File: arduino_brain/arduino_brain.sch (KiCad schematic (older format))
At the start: 42 parts, among them U1 R-78B5.0-1.5

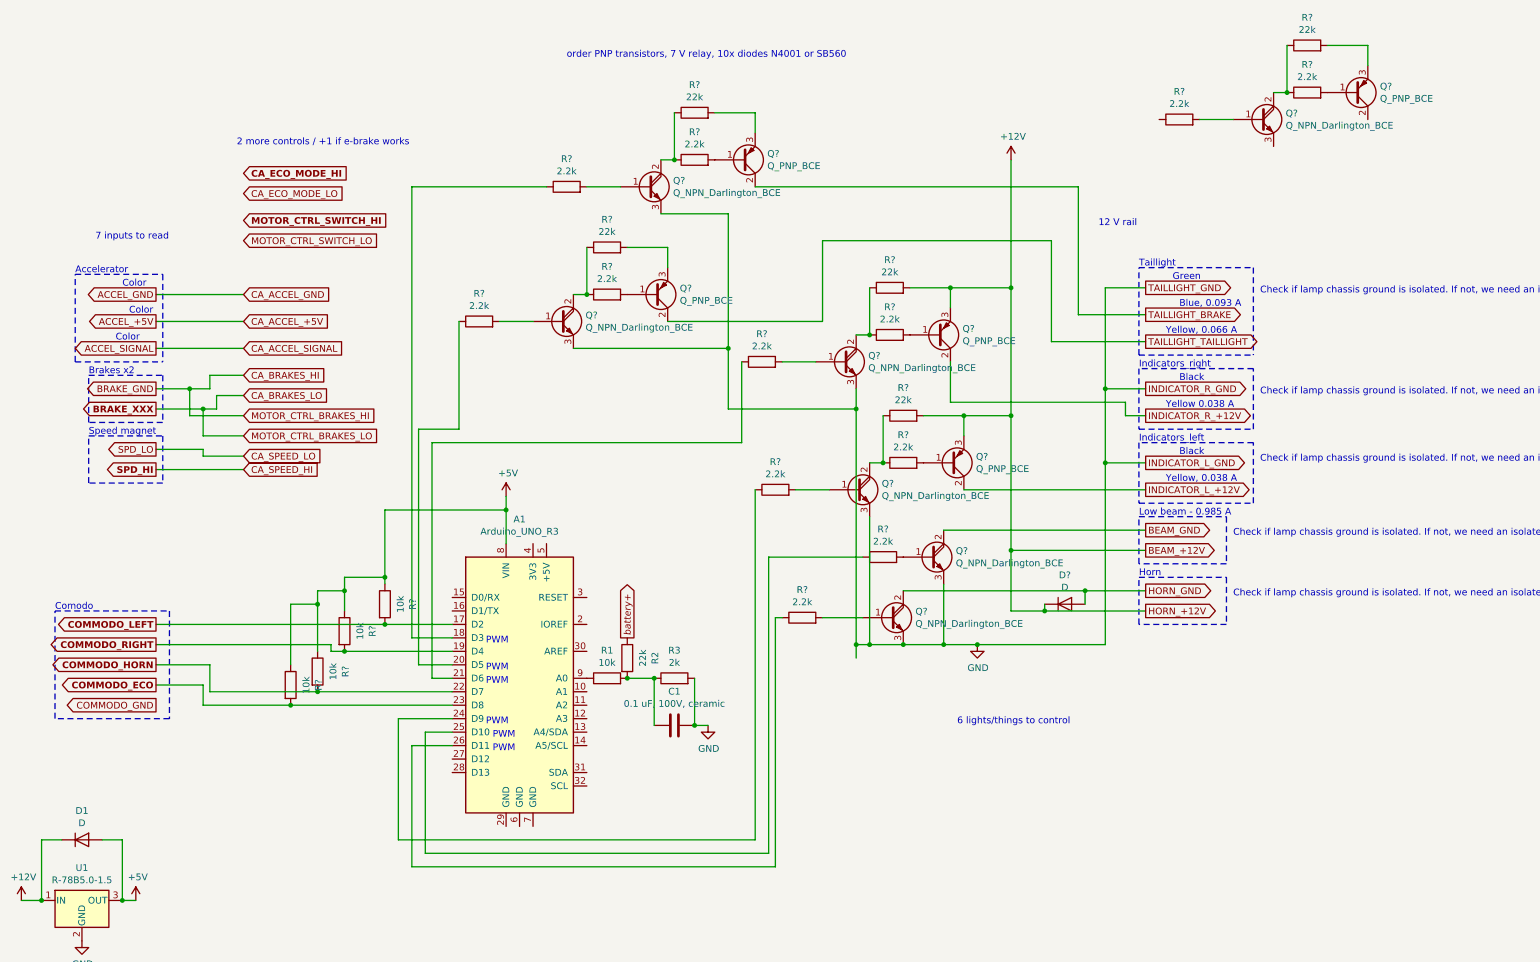
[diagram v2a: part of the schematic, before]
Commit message: Added 12V switching regulator, eco mode control and cleaned schematic
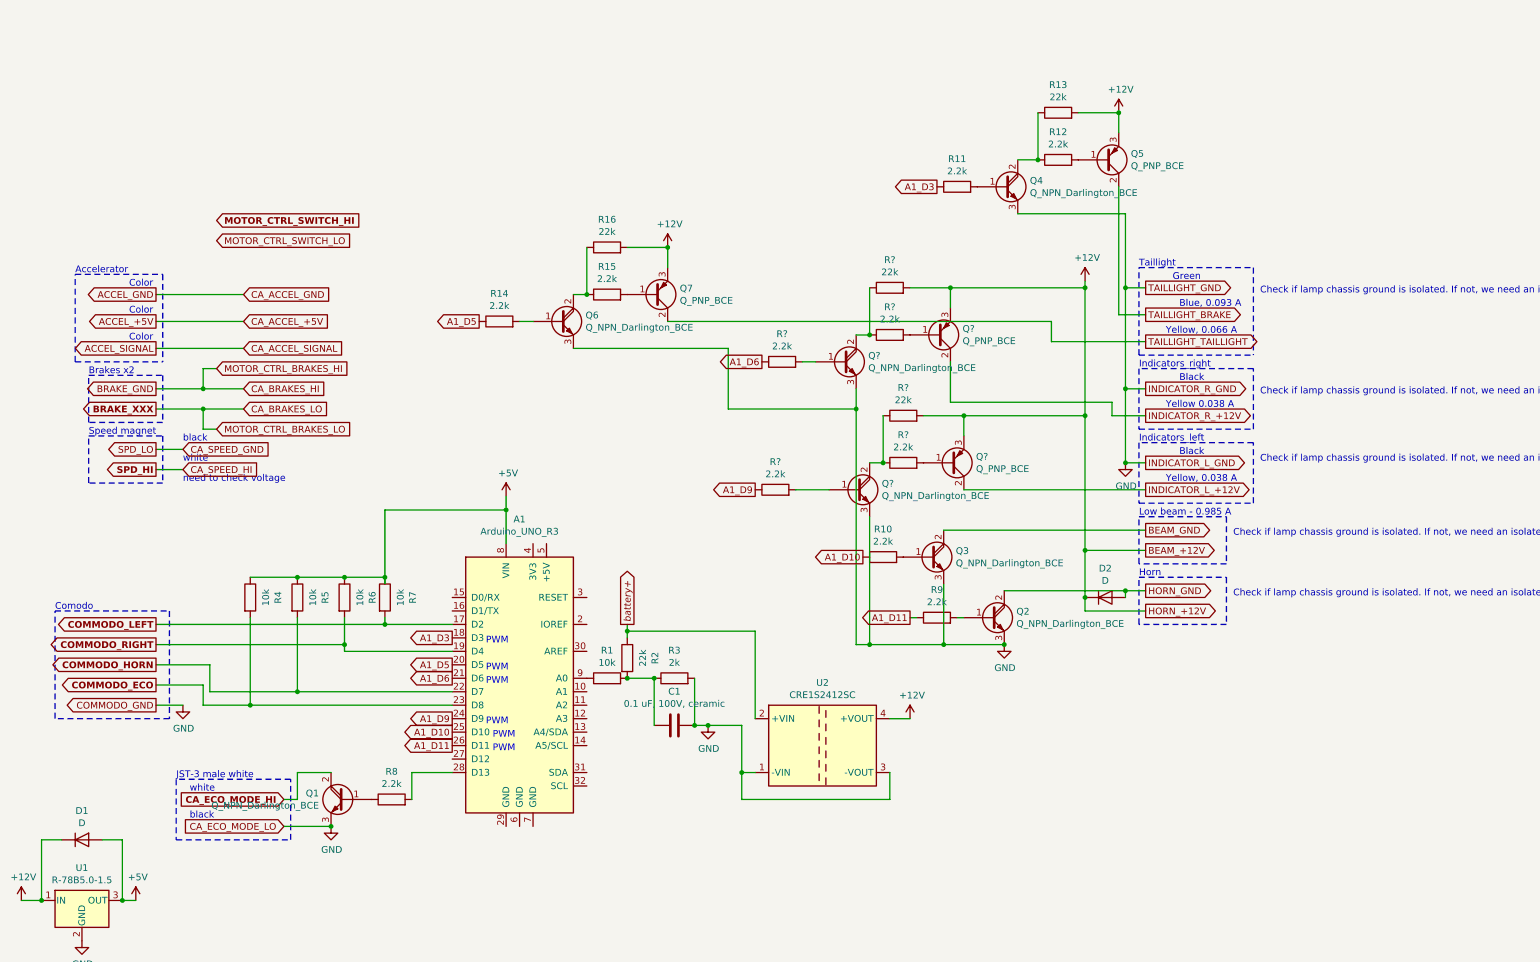
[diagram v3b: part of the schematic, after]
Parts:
- removed Q?: Q_NPN_Darlington_BCE, symbol Device:Q_NPN_Darlington_BCE
- removed Q?: Q_PNP_BCE, symbol Device:Q_PNP_BCE
- removed R? (x2): 2.2k, symbol Device:R
- removed R?: 22k, symbol Device:R
- added Q1: Q_NPN_Darlington_BCE, symbol Device:Q_NPN_Darlington_BCE
- added R8: 2.2k, symbol Device:R
- added U2: CRE1S2412SC, Converter_DCDC:Converter_DCDC_muRata_CRE1xxxxxxSC_THT, symbol Regulator_Switching:CRE1S2412SC
- gave numbers to parts that had none: 19
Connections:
- net +12V: now also Q5.3 (E), Q7.3 (E), R13.2, R16.2, U2.4 (+VOUT)
- net CA_ECO_MODE_HI: now also Q1.2 (C)
- net GND: now also Q1.3 (E), U2.1 (-VIN), U2.3 (-VOUT)
- net battery+: now also U2.2 (+VIN)
- net A1_D9: now reaches A1.24 (D9), R?.1
- net A1_D11: now reaches A1.26 (D11), R9.1
- net A1_D10: now reaches A1.25 (D10), R10.1
- net A1_D6: now reaches A1.21 (D6), R?.1
- net A1_D3: now reaches A1.18 (D3), R11.1
- net A1_D5: now reaches A1.20 (D5), R14.1
- net at A1.28 (D13): now also R8.2
- new net: Q1.1 (B), R8.1
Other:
- note added: "JST-3 male white"
- note added: "black"
- note added: "need to check voltage"
- note added: "white"
- note removed: "12 V rail"
- note removed: "2 more controls / +1 if e-brake works"
- note removed: "6 lights/things to control"
- note removed: "7 inputs to read"
- note removed: "order PNP transistors, 7 V relay, 10x diodes N4001 or SB560"
- moved on the sheet: D2, Q2, Q4, Q5, R11, R12, R13, R14, R4, R5, R6, R7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

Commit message: Cleaned up the notations
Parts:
- gave numbers to parts that had none: 11
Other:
- note added: "Black (2)"
- note added: "Green (3)"
- note added: "JST-3-F black"
- note added: "JST-3-F white"
- note added: "Red (1)"
- note added: "TODO: \n- wire the speed sensor\n- wire the start/stop"
- note added: "black (2)"
- note added: "white (3)"
- note removed: "9 free I/O\n15 I/O to have"
- note removed: "JST-3 male white"
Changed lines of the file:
@@
 $EndDescr
 $Comp
-L MCU_Module:Arduino_UNO_R3 A?
+L MCU_Module:Arduino_UNO_R3 A2
 U 1 1 5DFDE4CB
 P -1750 6050
-F 0 "A?" H -1750 7231 50  0000 C CNN
+F 0 "A2" H -1750 7231 50  0000 C CNN
 F 1 "Arduino_UNO_R3" H -1750 7140 50  0000 C CNN
 F 2 "Module:Arduino_UNO_R3" H -1600 5000 50  0001 L CNN
@@
 Text GLabel 1650 5700 0    50   Output ~ 0
 COMMODO_GND
-Text Notes -1100 5050 0    50   ~ 0
-9 free I/O\n15 I/O to have
 Text GLabel -2150 8050 2    50   Input ~ 0
 BLUEFRUIT_MOSI
@@
 	9000 5000 8550 5000
 $Comp
-L Device:Q_NPN_Darlington_BCE Q?
+L Device:Q_NPN_Darlington_BCE Q10
 U 1 1 5E0ABF98
 P 6850 4100
-F 0 "Q?" H 7040 4146 50  0000 L CNN
+F 0 "Q10" H 7040 4146 50  0000 L CNN
 F 1 "Q_NPN_Darlington_BCE" H 7040 4055 50  0000 L CNN
 F 2 "" H 7050 4200 50  0001 C CNN
@@
 $EndComp
 $Comp
-L Device:R R?
+L Device:R R20
 U 1 1 5E0AE97B
 P 6250 4100
-F 0 "R?" V 6457 4100 50  0000 C CNN
+F 0 "R20" V 6457 4100 50  0000 C CNN
 F 1 "2.2k" V 6366 4100 50  0000 C CNN
 F 2 "" V 6180 4100 50  0001 C CNN
@@
 Check if lamp chassis ground is isolated. If not, we need an isolated ground (not connecting battery ground with chassis ground!!!)
 $Comp
-L Device:Q_PNP_BCE Q?
+L Device:Q_PNP_BCE Q11
 U 1 1 5E0EA248
 P 7550 3900
-F 0 "Q?" H 7740 3854 50  0000 L CNN
+F 0 "Q11" H 7740 3854 50  0000 L CNN
 F 1 "Q_PNP_BCE" H 7740 3945 50  0000 L CNN
 F 2 "" H 7750 4000 50  0001 C CNN
@@
 $EndComp
 $Comp
-L Device:R R?
+L Device:R R21
 U 1 1 5E0EAF2D
 P 7200 3900
-F 0 "R?" V 7407 3900 50  0000 C CNN
+F 0 "R21" V 7407 3900 50  0000 C CNN
 F 1 "2.2k" V 7316 3900 50  0000 C CNN
 F 2 "" V 7130 3900 50  0001 C CNN
@@
 	7050 3900 6950 3900
 $Comp
-L Device:R R?
+L Device:R R22
 U 1 1 5E0FEFBE
 P 7200 3550
-F 0 "R?" V 7407 3550 50  0000 C CNN
+F 0 "R22" V 7407 3550 50  0000 C CNN
 F 1 "22k" V 7316 3550 50  0000 C CNN
 F 2 "" V 7130 3550 50  0001 C CNN
@@
 	7650 4100 9000 4100
 $Comp
-L Device:Q_NPN_Darlington_BCE Q?
+L Device:Q_NPN_Darlington_BCE Q8
 U 1 1 5E10C4F3
 P 6750 3150
-F 0 "Q?" H 6940 3196 50  0000 L CNN
+F 0 "Q8" H 6940 3196 50  0000 L CNN
 F 1 "Q_NPN_Darlington_BCE" H 6940 3105 50  0000 L CNN
 F 2 "" H 6950 3250 50  0001 C CNN
@@
 $EndComp
 $Comp
-L Device:R R?
+L Device:R R17
 U 1 1 5E10C4FD
 P 6300 3150
-F 0 "R?" V 6507 3150 50  0000 C CNN
+F 0 "R17" V 6507 3150 50  0000 C CNN
 F 1 "2.2k" V 6416 3150 50  0000 C CNN
 F 2 "" V 6230 3150 50  0001 C CNN
@@
 	6450 3150 6550 3150
 $Comp
-L Device:Q_PNP_BCE Q?
+L Device:Q_PNP_BCE Q9
 U 1 1 5E10C508
 P 7450 2950
-F 0 "Q?" H 7640 2904 50  0000 L CNN
+F 0 "Q9" H 7640 2904 50  0000 L CNN
 F 1 "Q_PNP_BCE" H 7640 2995 50  0000 L CNN
 F 2 "" H 7650 3050 50  0001 C CNN
@@
 $EndComp
 $Comp
-L Device:R R?
+L Device:R R18
 U 1 1 5E10C512
 P 7100 2950
-F 0 "R?" V 7307 2950 50  0000 C CNN
+F 0 "R18" V 7307 2950 50  0000 C CNN
 F 1 "2.2k" V 7216 2950 50  0000 C CNN
 F 2 "" V 7030 2950 50  0001 C CNN
@@
 	6950 2950 6850 2950
 $Comp
-L Device:R R?
+L Device:R R19
 U 1 1 5E10C51D
 P 7100 2600
-F 0 "R?" V 7307 2600 50  0000 C CNN
+F 0 "R19" V 7307 2600 50  0000 C CNN
 F 1 "22k" V 7216 2600 50  0000 C CNN
 F 2 "" V 7030 2600 50  0001 C CNN
@@
 	1800 6700 2650 6700
 Text Notes 1900 6350 0    50   ~ 0
-white
+white (3)
 Text Notes 1900 6550 0    50   ~ 0
-black
+black (2)
 Text Notes 1800 6250 0    50   ~ 0
-JST-3 male white
+JST-3-F white
 Wire Notes Line
 	1800 6250 1800 6700
@@
 Connection ~ 8850 3900
 $Comp
-L power:GND #PWR?
+L power:GND #PWR0113
 U 1 1 5E50ECA0
 P 8850 3900
-F 0 "#PWR?" H 8850 3650 50  0001 C CNN
+F 0 "#PWR0113" H 8850 3650 50  0001 C CNN
 F 1 "GND" H 8855 3727 50  0000 C CNN
 F 2 "" H 8850 3900 50  0001 C CNN
@@
 	7550 2600 8550 2600
 $Comp
-L power:+12V #PWR?
+L power:+12V #PWR0114
 U 1 1 5E635F99
 P 8800 1300
-F 0 "#PWR?" H 8800 1150 50  0001 C CNN
+F 0 "#PWR0114" H 8800 1150 50  0001 C CNN
 F 1 "+12V" H 8815 1473 50  0000 C CNN
 F 2 "" H 8800 1300 50  0001 C CNN
@@
 Connection ~ 8800 1300
 $Comp
-L power:+12V #PWR?
+L power:+12V #PWR0115
 U 1 1 5E6365E0
 P 5450 2300
-F 0 "#PWR?" H 5450 2150 50  0001 C CNN
+F 0 "#PWR0115" H 5450 2150 50  0001 C CNN
 F 1 "+12V" H 5465 2473 50  0000 C CNN
 F 2 "" H 5450 2300 50  0001 C CNN
@@
 Wire Wire Line
 	5450 2850 8300 2850
+Text Notes 700  750  0    50   ~ 0
+TODO: \n- wire the speed sensor\n- wire the start/stop
+Text Notes 2300 2600 0    50   ~ 0
+Black (2)
+Text Notes 2300 2800 0    50   ~ 0
+Red (1)
+Text Notes 2300 3000 0    50   ~ 0
+Green (3)
+Wire Notes Line
+	3050 3150 2200 3150
+Wire Notes Line
+	2200 3150 2200 2500
+Wire Notes Line
+	2200 2500 3050 2500
+Wire Notes Line
+	3050 2500 3050 3150
+Text Notes 2200 2500 0    50   ~ 0
+JST-3-F black
 $EndSCHEMATC

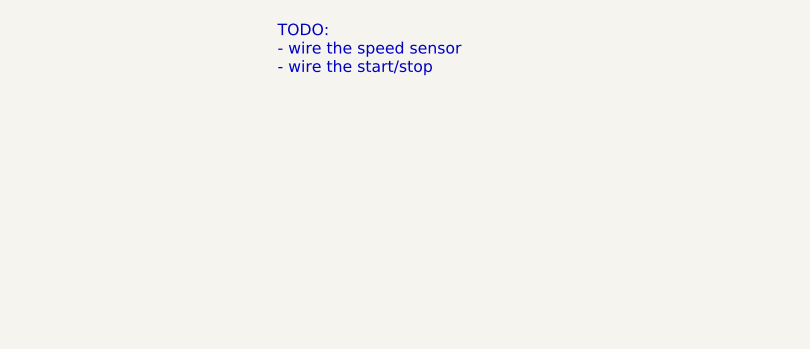
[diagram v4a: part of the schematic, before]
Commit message: Cleaned up horn state machine design
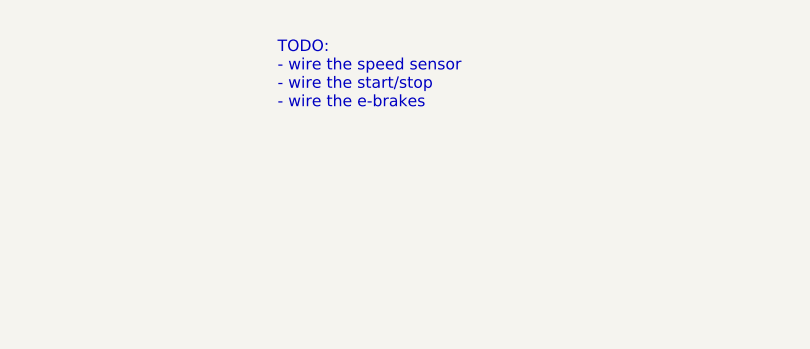
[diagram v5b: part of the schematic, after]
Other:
- note added: "TODO: \n- wire the speed sensor\n- wire the start/stop\n- wire the e-brakes"
- note removed: "TODO: \n- wire the speed sensor\n- wire the start/stop"
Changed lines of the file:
@@
 Wire Wire Line
 	5450 2850 8300 2850
-Text Notes 700  750  0    50   ~ 0
-TODO: \n- wire the speed sensor\n- wire the start/stop
+Text Notes 700  900  0    50   ~ 0
+TODO: \n- wire the speed sensor\n- wire the start/stop\n- wire the e-brakes
 Text Notes 2300 2600 0    50   ~ 0
 Black (2)

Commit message: Better transistors, 5 to 7V for Arduino rail and duplicate brake and speed outputs.
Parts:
- removed C1: 0.1 uF, 100V, ceramic, symbol Device:C
- removed D1: D, symbol Device:D
- removed R1: 10k, symbol Device:R
- removed R2: 22k, symbol Device:R
- removed R3: 2k, symbol Device:R
- removed U1: R-78B5.0-1.5, Converter_DCDC:Converter_DCDC_RECOM_R-78B-2.0_THT, symbol Regulator_Switching:R-78B5.0-2.0
- added C?: 220uF, symbol Device:C_Small
- added C?: 27 uF 40 mOhm, symbol Device:CP1_Small
- added C?: 820 pF, symbol Device:C_Small
- added C? (x2): 100 uF 150 mOhm, symbol Device:CP1_Small
- added C?: 0.1 uF, 100V, symbol Device:C
- added D?: 550mV, 2A, symbol Device:D_Schottky_Small
- added L?: 33uH, 33mO, symbol Device:L_Small
- added R?: 1k, symbol Device:R_Small
- added R?: 4.64k, symbol Device:R_Small
- added R?: 10k, symbol Device:R
- added R?: 4M7, 1%, CFR-25JB-52-22K, symbol Device:R
- added R?: 390k, 1%, symbol Device:R
- added U?: Adafruit_2719(SPI), symbol User_library:Adafruit_2719(SPI)
- added U?: LM2596T-ADJ, Package_TO_SOT_THT:TO-220-5_P3.4x3.7mm_StaggerOdd_Lead3.8mm_Vertical, symbol Regulator_Switching:LM2596T-ADJ
- A1: symbol MCU_Module:Arduino_UNO_R3 -> User_library:Arduino_UNO_R3_annot
- D2: symbol Device:D -> Device:D_Small
- Q1, Q10, Q4, Q6, Q8: value Q_NPN_Darlington_BCE -> 2N3904; footprint (none) -> Package_TO_SOT_THT:TO-92_Inline; symbol Device:Q_NPN_Darlington_BCE -> Transistor_BJT:2N3904
- Q11, Q5, Q7, Q9: value Q_PNP_BCE -> 2N3906; footprint (none) -> Package_TO_SOT_THT:TO-92_Inline; symbol Device:Q_PNP_BCE -> Transistor_BJT:2N3906
- Q2, Q3: value Q_NPN_Darlington_BCE -> TIP120; footprint (none) -> Package_TO_SOT_THT:TO-220-3_Vertical; symbol Device:Q_NPN_Darlington_BCE -> Transistor_BJT:TIP120
- R10, R9: value 2.2k -> 3.3k; symbol Device:R -> Device:R_Small
- R11, R14, R17, R18, R20, R21: value 2.2k -> 4k7; symbol Device:R -> Device:R_Small
- R12, R15: value 2.2k -> 1k; symbol Device:R -> Device:R_Small
- R13, R16: value 22k -> 4k7; symbol Device:R -> Device:R_Small
- R19, R22: symbol Device:R -> Device:R_Small
- R8: value 2.2k -> 10k
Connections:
- net battery+ is gone; now on net +BATT: U2.2 (+VIN)
- net +12V: now also Q11.1 (E), Q5.1 (E), Q7.1 (E), Q9.1 (E), C?.1, U?.1 (VIN); no longer Q11.3 (E), Q5.3 (E), Q7.3 (E), Q9.3 (E)
- net +5V: now also A1.5 (+5V); no longer A1.8 (VIN)
- net +BATT: no longer A2.8 (VIN)
- net A1_D10: now also U?.15 (CS); no longer R10.1
- net A1_D11: now also U?.8 (Data1); no longer R9.1
- net A1_D3: now also R9.1; no longer R11.1
- net A1_D5: no longer R14.1
- net A1_D6: now also R11.1; no longer R17.1
- net A1_D9: now also U?.16 (RESET); no longer R20.1
- net CA_ECO_MODE_HI: now also Q1.3 (C); no longer Q1.2 (C)
- net INDICATOR_L_+12V: now also Q11.3 (C); no longer Q11.2 (C)
- net INDICATOR_R_+12V: now also Q9.3 (C); no longer Q9.2 (C)
- net TAILLIGHT_BRAKE: now also Q5.3 (C); no longer Q5.2 (C)
- net TAILLIGHT_TAILLIGHT: now also Q7.3 (C); no longer Q7.2 (C)
- net A1_A4: now reaches A2.13 (A4/SDA)
- net A1_A4: now also A1.13 (A4/SDA_I2C)
- net A1_A5: now reaches A2.14 (A5/SCL)
- net A1_A5: now also A1.14 (A5/SCL_I2C)
- net at R20.2: now also Q10.2 (B); no longer Q10.1 (B)
- net at R21.1, R22.1: now also Q10.3 (C); no longer Q10.2 (C)
- net at R21.2: now also Q11.2 (B); no longer Q11.1 (B)
- net A1_A0: now reaches A1.9 (A0)
- net A1_A0: now also R?.1
- net at R17.2: now also Q8.2 (B); no longer Q8.1 (B)
- net at R18.1, R19.1: now also Q8.3 (C); no longer Q8.2 (C)
- net at R18.2: now also Q9.2 (B); no longer Q9.1 (B)
- net at R11.2: now also Q4.2 (B); no longer Q4.1 (B)
- net at R12.1, R13.1: now also Q4.3 (C); no longer Q4.2 (C)
- net at R12.2: now also Q5.2 (B); no longer Q5.1 (B)
- net -BATT: now reaches Q6.1 (E), R14.2
- net -BATT: now also A1.7 (GND), A2.7 (GND), Q10.1 (E), Q2.3 (E), Q3.3 (E), Q4.1 (E), Q6.2 (B), Q8.1 (E), U2.1 (-VIN), U2.3 (-VOUT), C?.2, C?.2, C?.2, C?.2, C?.2, D?.2 (A), R?.1, R?.2, U?.1 (GND), U?.3 (GND)
- net at R15.1, R16.1: now also Q6.3 (C); no longer Q6.2 (C)
- net at R15.2: now also Q7.2 (B); no longer Q7.1 (B)
- net A1_A1: now reaches A1.10 (A1)
- net A1_A2: now reaches A1.11 (A2)
- net A1_A2: now also R17.1
- net A1_A3: now reaches A1.12 (A3)
- net A1_A3: now also R20.1
- net A1_D0: now reaches A1.15 (D0/RX_UART)
- net A1_D0: now also R4.2
- net A1_D1: now reaches A1.16 (D1/TX_UART)
- net A1_D1: now also R5.2
- net A1_D12: now reaches A1.27 (D12/MISO_SPI)
- net at R8.2: now also Q1.2 (B); no longer A1.28 (D13)
- net +3V3: now reaches A1.4 (3V3)
- net +3V3: now also C?.1, U?.2 (PWR(3V))
- net A1_D7: now reaches R8.1
- net A1_D7: now also A1.22 (D7); no longer Q1.1 (B)
- net COMMODO_ECO renamed A1_D8
- net A1_D8: now also U?.4 (DC); no longer R4.2
- removed net COMMODO_HORN: A1.22 (D7), R5.2
- net COMMODO_LEFT renamed A1_D2
- net A1_D2: now also R6.2; no longer R7.2
- net COMMODO_RIGHT renamed A1_D4
- net A1_D4: now also R7.2; no longer R6.2
- removed net GND: A2.7 (GND), Q1.3 (E), Q10.3 (E), Q2.3 (E), Q3.3 (E), Q4.3 (E), Q6.3 (E), Q8.3 (E), U2.1 (-VIN), U2.3 (-VOUT)
- new net: D?.1 (K), L?.1, U?.2 (OUT)
- new net: C?.1, R?.1, R?.2, U?.4 (FB)
- new net: C?.1, R?.1, R?.2, R?.2
- new net +7.5V: A1.8 (VIN), A2.8 (VIN), C?.1, C?.1, C?.2, L?.2, R?.2
- new net A1_D13: A1.28 (D13/SCK_SPI/LED), U?.7 (Data0)
- new net A2_XX: R10.1, R14.1
- new net CA_ECO_MODE_GND: Q1.1 (E)
- new net CA_V+: R?.1
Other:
- note added: "(1) Red"
- note added: "(2) Black"
- note added: "(2?) Blue"
- note added: "(3) Green"
- note added: "(3) White"
- note added: "(4) Blue"
- note added: "(X) Black"
- note added: "(X) Red"
- note added: "(X) XXX"
- note added: "Brakes"
- note added: "Comodo\nblue, white, brown soldered together as GND\ngreen cut off"
- note added: "JST-2-M black"
- note added: "JST-4-F black"
- note added: "Screen"
- note added: "TODO: \n- build test circuitry w/ Darlington, n-FET and evaluate (T, current drawn, Voltage drop, efficiency).\n- wire the start/stop"
- note added: "To low-level coupler"
- note added: "battery"
- note added: "beam"
- note added: "blue"
- note added: "brake"
- note added: "brakes"
- note added: "commodo"
- note added: "eco"
- note added: "grey"
- note added: "horn"
- note added: "left"
- note added: "red"
- note added: "right"
- note added: "shunt/Other Arduino"
- note added: "speed"
- note added: "taillight"
- note added: "yellow"
- note removed: "Black (2)"
- note removed: "Brakes x2"
- note removed: "Check if lamp chassis ground is isolated. If not, we need an isolated ground (not connecting battery ground with chassis ground!!!)"
- note removed: "Color"
- note removed: "Comodo"
- note removed: "Green (3)"
- note removed: "PWM"
- note removed: "Red (1)"
- note removed: "TODO: \n- wire the speed sensor\n- wire the start/stop\n- wire the e-brakes"
- note removed: "black (2)"
- note removed: "need to check voltage"
- note removed: "white"
- note removed: "white (3)"
- moved on the sheet: A1, D2, Q11, Q5, Q7, Q9, R10, R11, R12, R13, R14, R15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
